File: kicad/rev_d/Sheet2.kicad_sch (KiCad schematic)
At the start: 213 parts, among them J10 vg_old, J5 external clock, J6 JUMPER, J8 JUMPER, J9 JUMPER, Q2 QUARTZ, Q3 QUARTZ32768, U1 74HCT1G04, X10 ST-214C, X11 KEYB-MOUSE, X12 IDC20, X13 USB_C, X14 AAFP/AC97 audio, X15 PLB2-2, X16 PLB1-4I, X17 PLB1-4I, X18 PLB1-4I, X19 AVR pgm conn, X20 PLB1-4I, X4 IDC10M, X5 IDC10M, X6 RS232_9

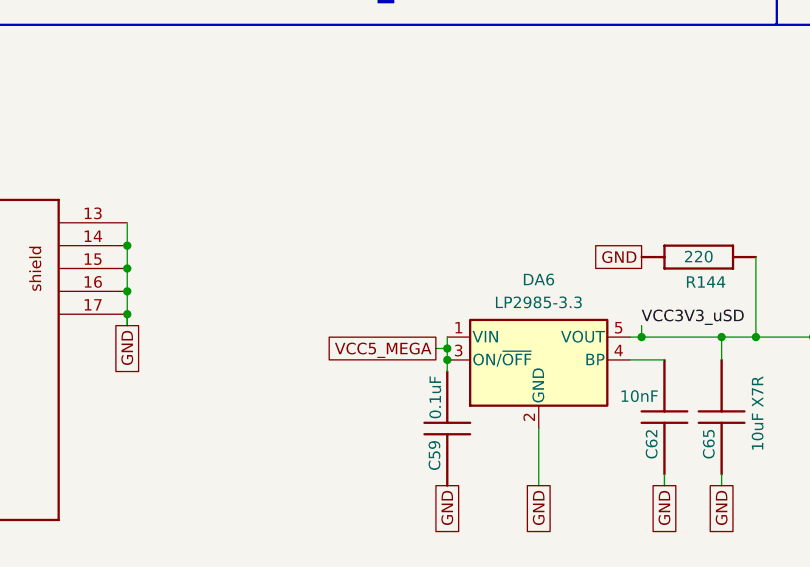
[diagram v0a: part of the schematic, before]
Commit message: pentevo: rev D: change uSD card LDO to tpa7a2033, which is drop-in replacement for lp2985 with increased max current
git-svn-id: svn://localhost/local-pentevo@1215 c6c76956-fad2-4150-a3a9-ea0a427205ba
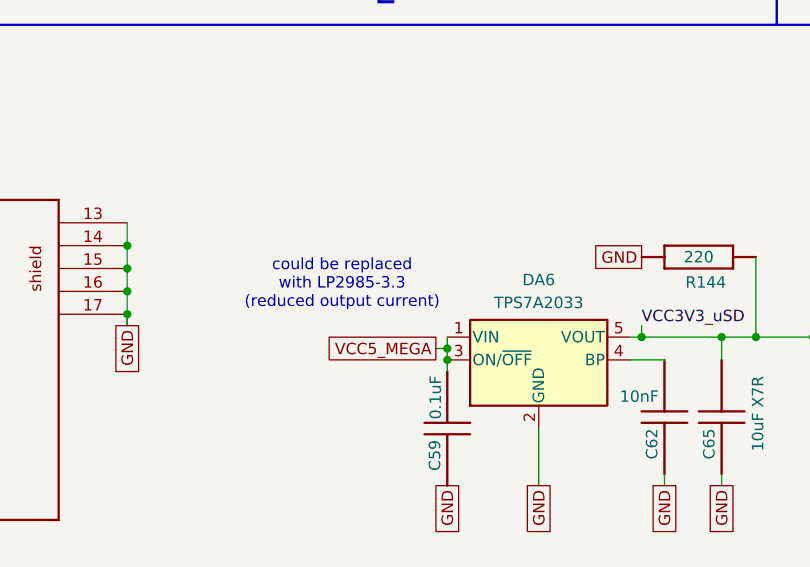
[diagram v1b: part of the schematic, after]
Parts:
- DA6: value LP2985-3.3 -> TPS7A2033
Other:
- note added: "could be replaced with LP2985-3.3 (reduced output current)"
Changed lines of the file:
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@@
 		)
 	)
+	(text "could be replaced\nwith LP2985-3.3\n(reduced output current)"
+		(exclude_from_sim no)
+		(at 408.686 84.328 0)
+		(effects
+			(font
+				(size 1.27 1.27)
+			)
+		)
+	)
 	(text "of"
 		(exclude_from_sim no)
@@
 			)
 		)
-		(property "Value" "LP2985-3.3"
+		(property "Value" "TPS7A2033"
 			(at 430.53 86.36 0)
 			(effects

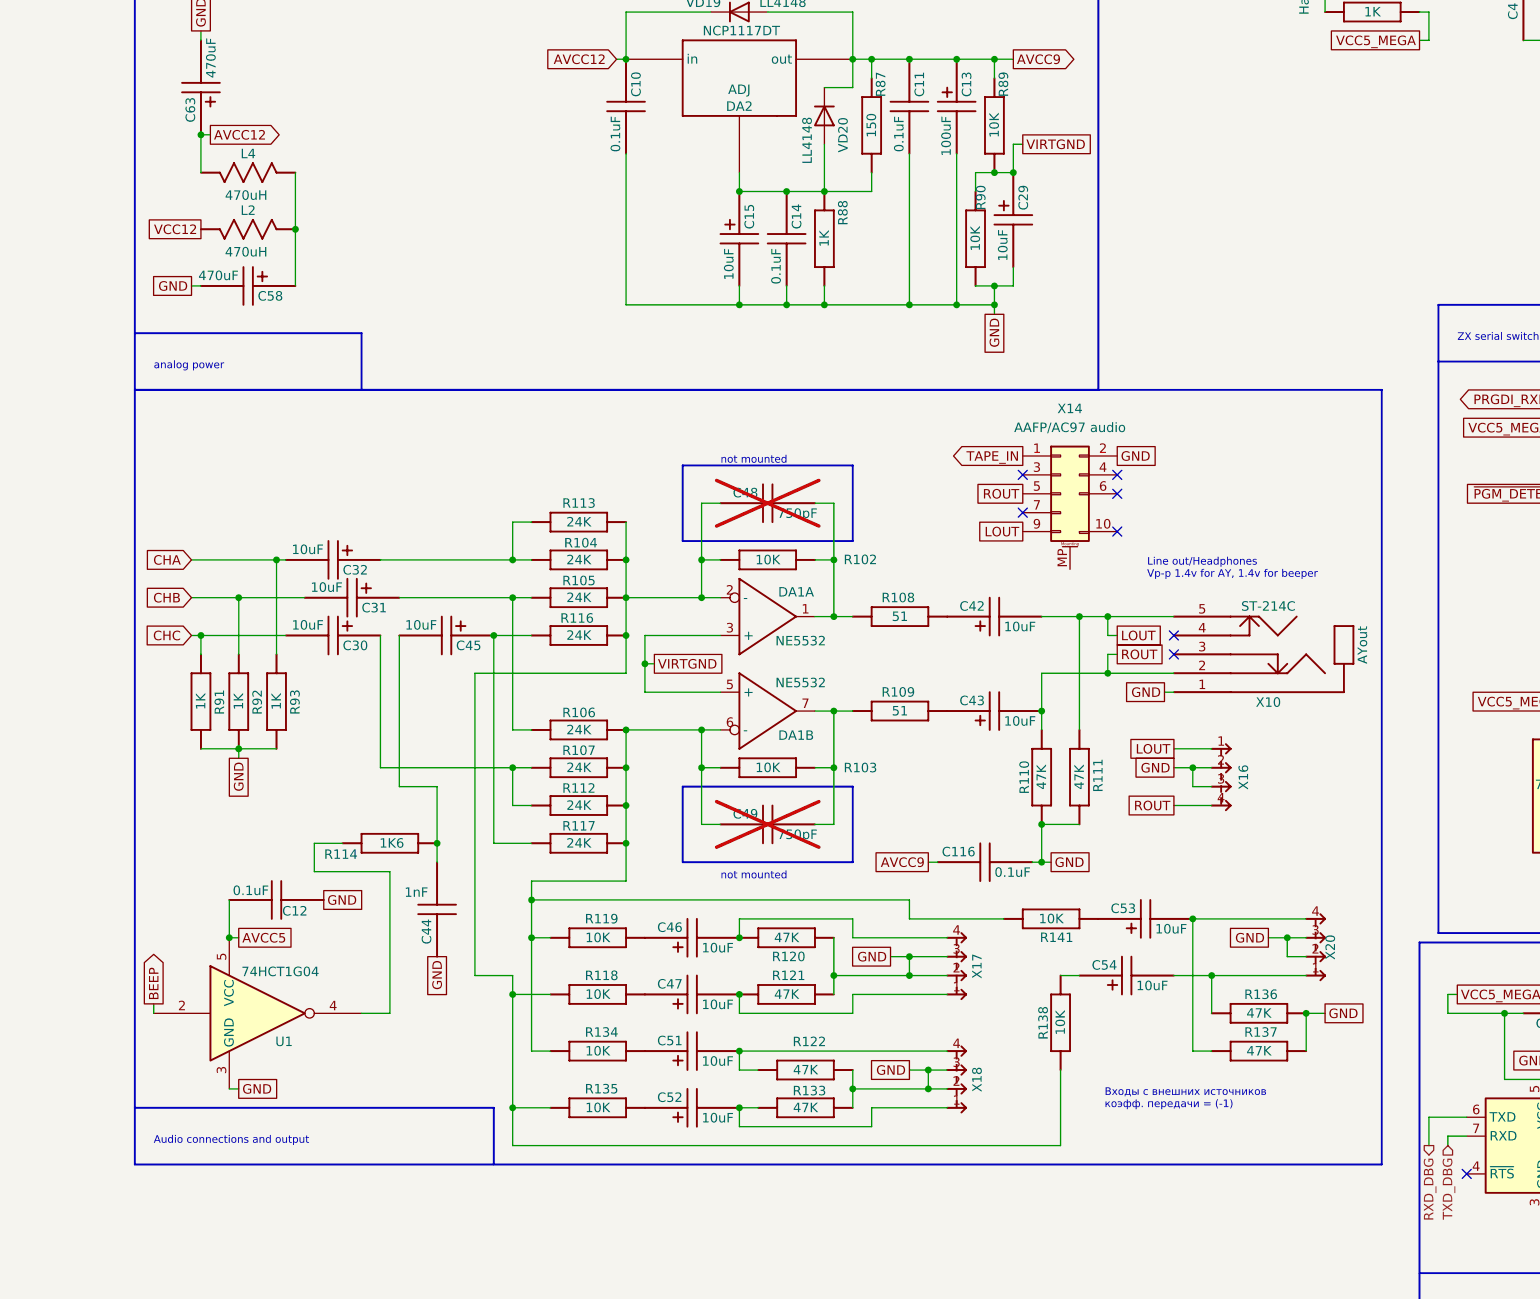
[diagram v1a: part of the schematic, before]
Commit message: pentevo: rev D: start redoing audio part (WIP)
git-svn-id: svn://localhost/local-pentevo@1219 c6c76956-fad2-4150-a3a9-ea0a427205ba
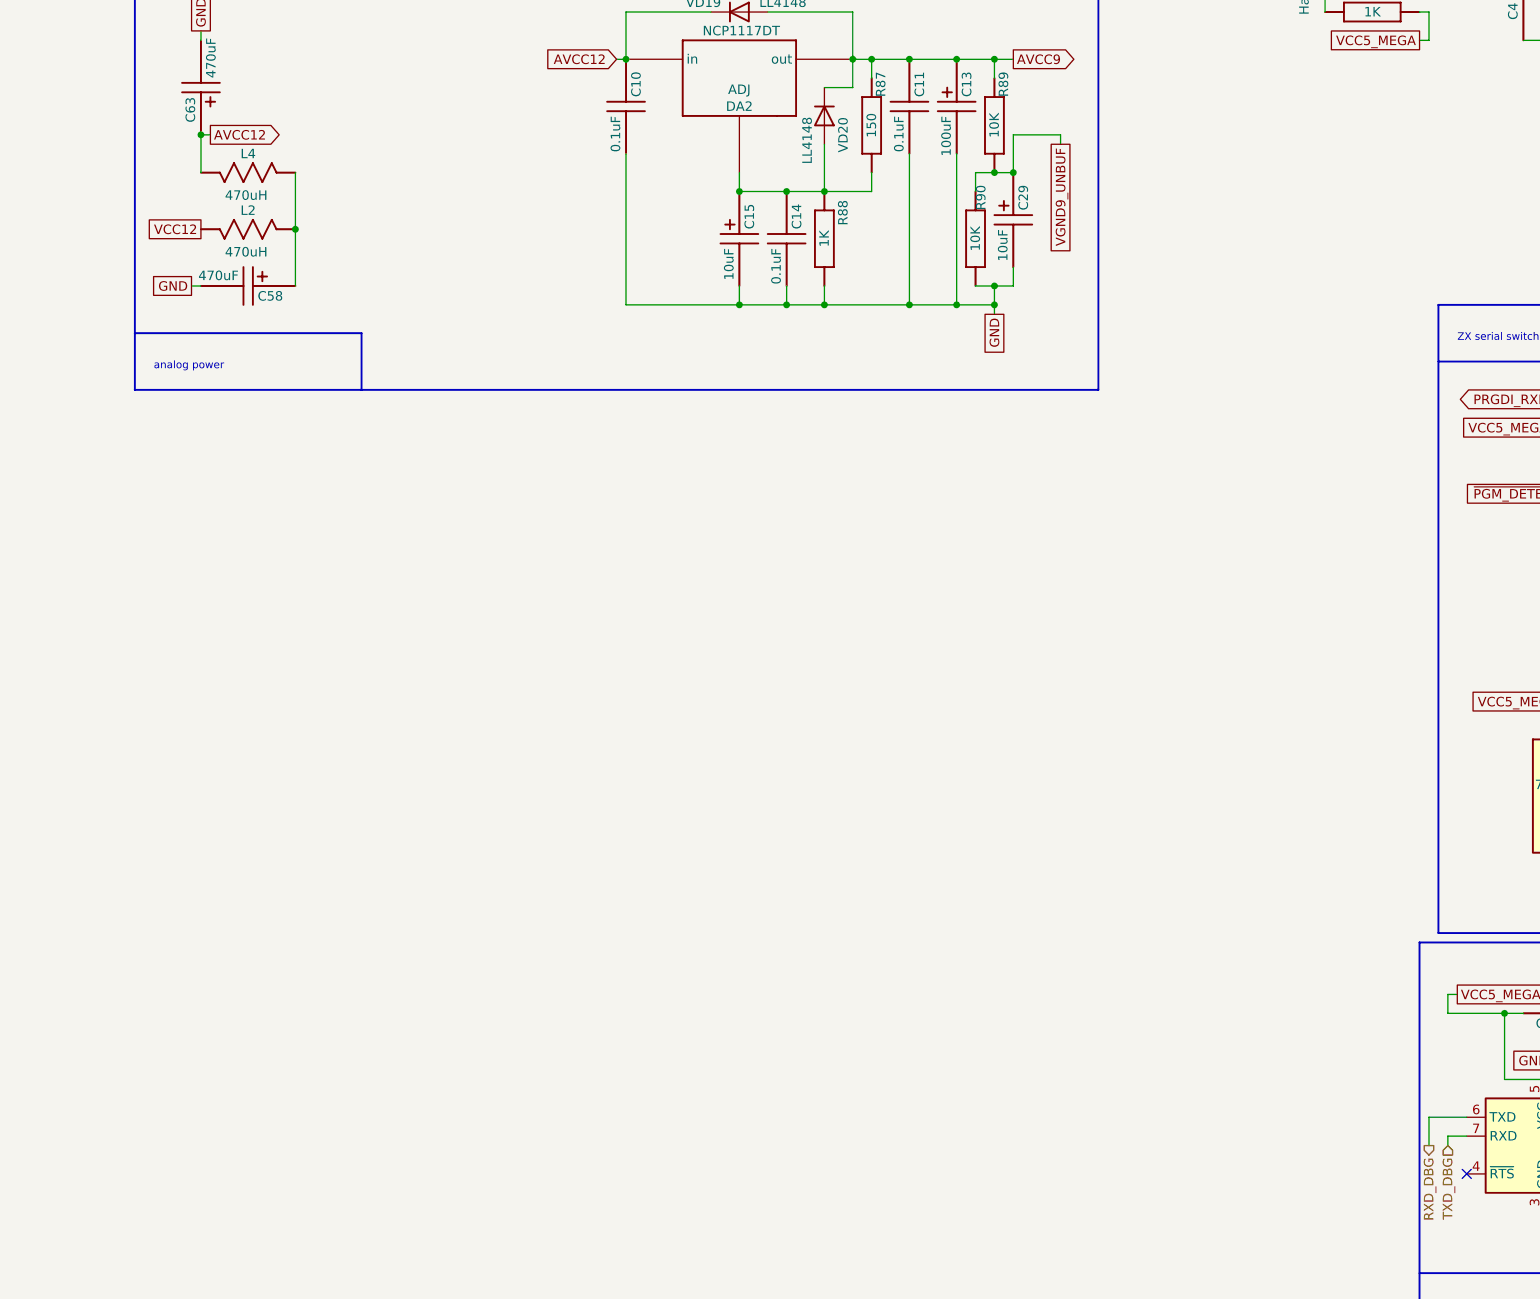
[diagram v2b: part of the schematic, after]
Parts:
- removed C116: 0.1uF, C-CHIP, symbol eva-altium-import:Sheet2_3_CAPCHIP
- removed C12: 0.1uF, C-CHIP, symbol eva-altium-import:Sheet2_0_CAPCHIP
- removed C30, C31, C32, C45: 10uF, EC-CHIP, symbol eva-altium-import:Sheet2_2_ECAPCHIP
- removed C42, C43, C46, C47, C51, C52, C53, C54: 10uF, EC-CHIP, symbol eva-altium-import:Sheet2_0_ECAPCHIP
- removed C44: 1nF, C-CHIP, symbol eva-altium-import:Sheet2_1_CAPCHIP
- removed C48, C49: 750pF, C-CHIP, symbol eva-altium-import:Sheet2_0_CAPCHIP
- removed DA1: NE5532, SO8, symbol eva-altium-import:Sheet2_0_NE5532
- removed R102: 10K, R-CHIP, symbol eva-altium-import:Sheet2_2_mirrored_RESCHIP
- removed R103, R118, R119, R134, R135: 10K, R-CHIP, symbol eva-altium-import:Sheet2_0_RESCHIP
- removed R104, R105, R113: 24K, R-CHIP, symbol eva-altium-import:Sheet2_0_RESCHIP
- removed R106, R107, R112, R116, R117: 24K, R-CHIP, symbol eva-altium-import:Sheet2_2_mirrored_RESCHIP
- removed R108, R109: 51, R-CHIP, symbol eva-altium-import:Sheet2_0_RESCHIP
- removed R110, R111: 47K, R-CHIP, symbol eva-altium-import:Sheet2_3_RESCHIP
- removed R114: 1K6, R-CHIP, symbol eva-altium-import:Sheet2_2_mirrored_RESCHIP
- removed R120, R121, R122, R133, R136, R137: 47K, R-CHIP, symbol eva-altium-import:Sheet2_0_RESCHIP
- removed R138: 10K, R-CHIP, symbol eva-altium-import:Sheet2_3_RESCHIP
- removed R141: 10K, R-CHIP, symbol eva-altium-import:Sheet2_2_RESCHIP
- removed R91, R92, R93: 1K, R-CHIP, symbol eva-altium-import:Sheet2_3_RESCHIP
- removed U1: 74HCT1G04, Package_TO_SOT_SMD:SOT-23-5_HandSoldering, symbol 74xGxx:74AHC1G04
- removed X10: ST-214C, ST-214C, symbol eva-altium-import:Sheet2_2_ST-214C
- removed X14: AAFP/AC97 audio, symbol Connector_Generic_MountingPin:Conn_2Rows-09Pins_MountingPin
- removed X16: PLB1-4I, PLB1-4I, symbol eva-altium-import:Sheet2_0_PLB1-4I
- removed X17, X18, X20: PLB1-4I, PLB1-4I, symbol eva-altium-import:Sheet2_2_mirrored_PLB1-4I
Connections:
- net VIRTGND renamed VGND9_UNBUF
- no-connect marks 29 -> 22
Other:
- note removed: "Audio connections and output"
- note removed: "not mounted"

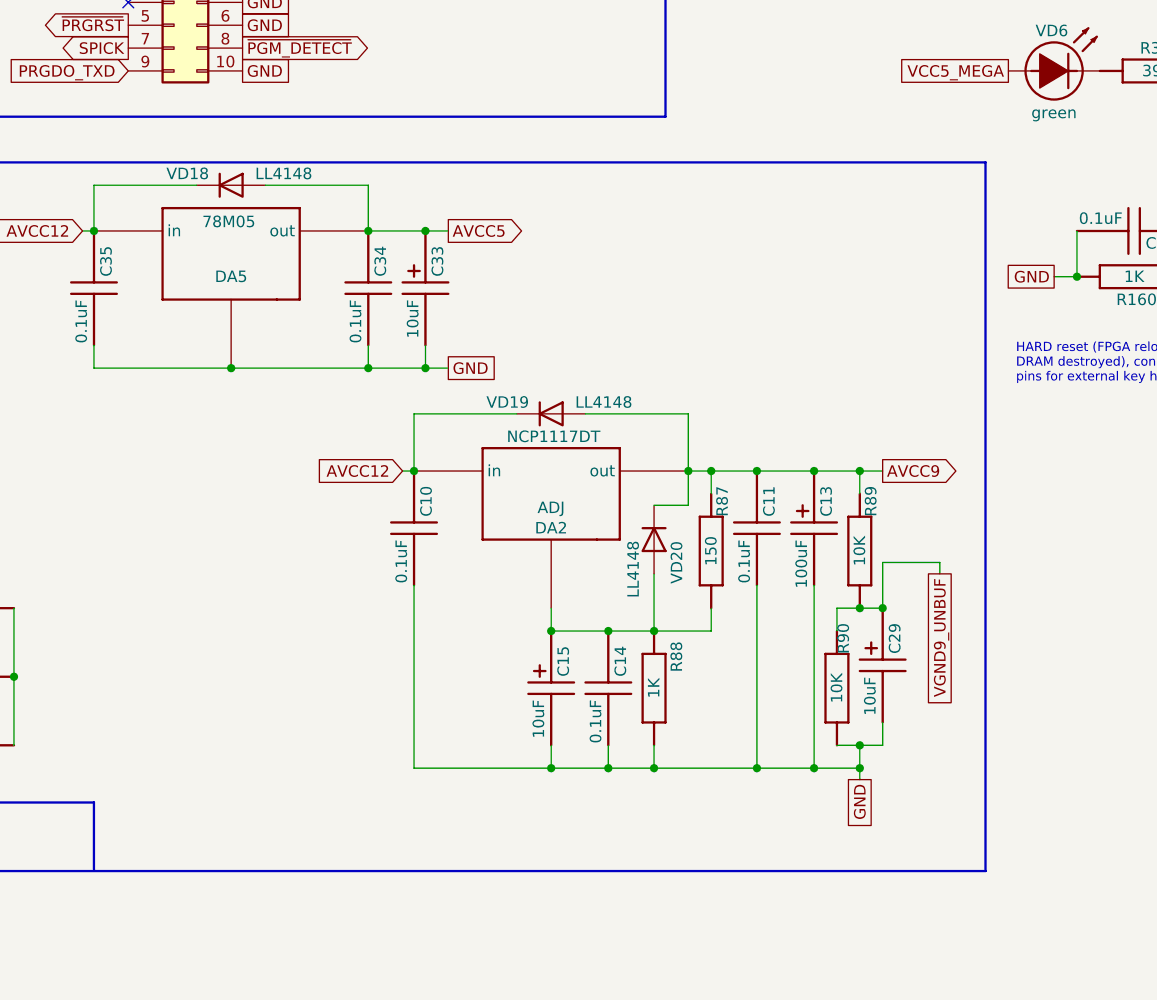
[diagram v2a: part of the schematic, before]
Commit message: pentevo: rev D: redoing audio (WIP), add reverse diodes to linear regulators
git-svn-id: svn://localhost/local-pentevo@1221 c6c76956-fad2-4150-a3a9-ea0a427205ba
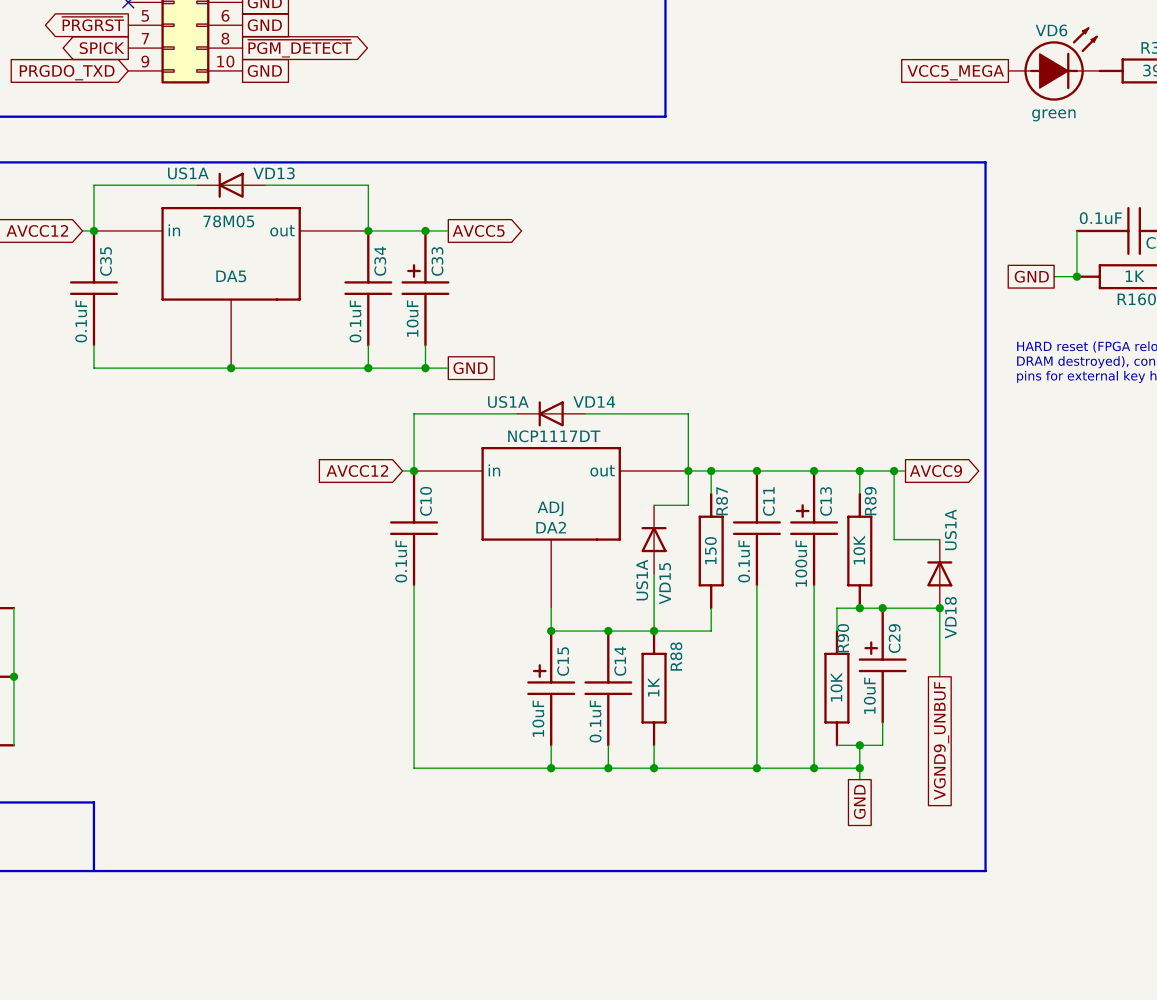
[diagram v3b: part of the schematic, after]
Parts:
- removed VD18, VD19, VD20: LL4148, Diode_SMD:D_MiniMELF_Handsoldering, symbol Diode:LL4148
- added VD13, VD14, VD15, VD18: US1A, Diode_SMD:D_SMA, symbol Diode:US1A
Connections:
- net AVCC12: now also VD13.1 (K), VD14.1 (K)
- net AVCC5: now also VD13.2 (A)
- net AVCC9: now also VD14.2 (A), VD15.1 (K), VD18.1 (K)
- net VGND9_UNBUF: now also VD18.2 (A)
- net at C14.1, C15.1, DA2.1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: now also VD15.2 (A)
